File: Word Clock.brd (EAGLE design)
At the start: 32 x 32 mm, 13 parts, among them IC1 DS3231/SO, U1 ATMEGA328P-AU

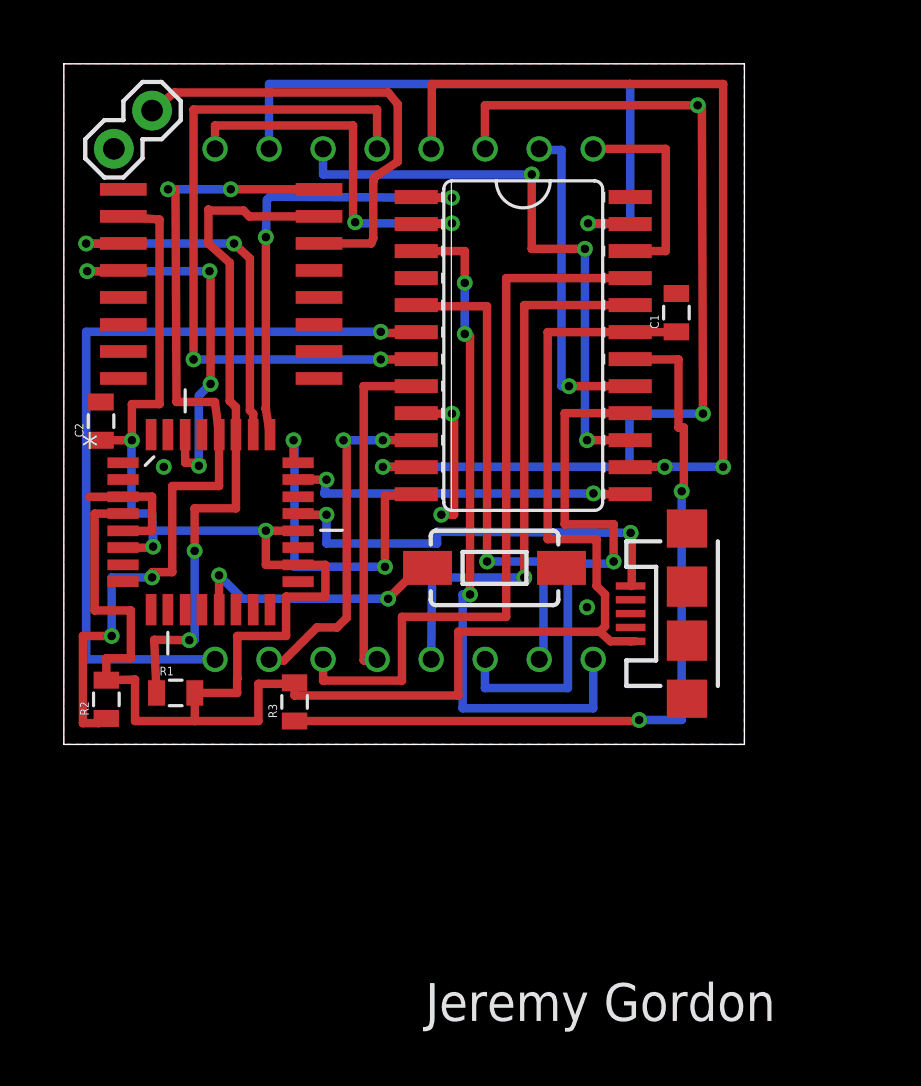
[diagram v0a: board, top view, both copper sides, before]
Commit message: Removed MAX7219, driving with raw atmega.
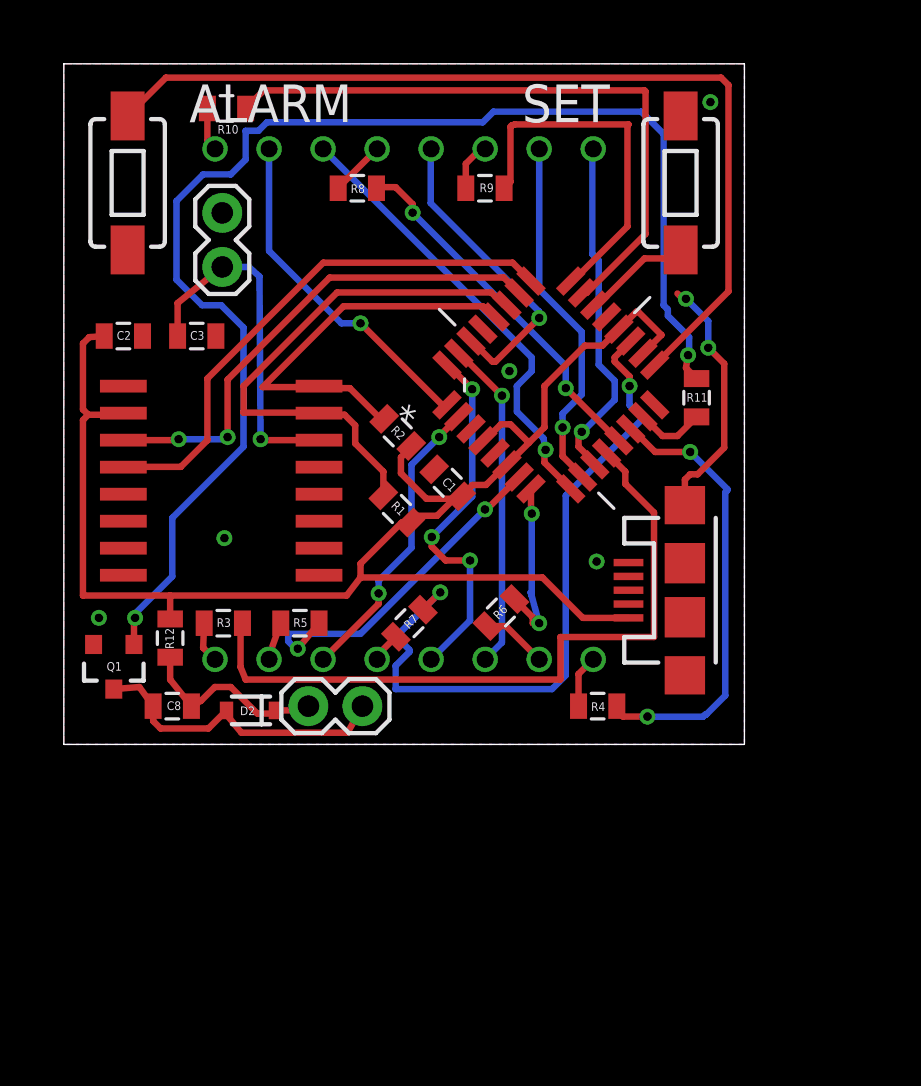
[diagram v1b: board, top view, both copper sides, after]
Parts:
- removed U$1: MAX7219CWG, max7219:SO24L
- added C3, C8: 0.1uF, SparkFun-Capacitors:0805
- added D2: 1N4001, SparkFun-DiscreteSemi:SOD-323
- added JP3: M02PTH, SparkFun-Connectors:1X02
- added Q1: MMBT2222A, SparkFun-DiscreteSemi:SOT23-3
- added R10, R4, R5, R6, R7, R8, R9: 330, SparkFun-Resistors:0805
- added R11: 1k, SparkFun-Resistors:0805
- added R12: 33, SparkFun-Resistors:0805
- added S2: SWITCH-MOMENTARY-2SMD-1101NE, SparkFun-Electromechanical:TACTILE-SWITCH-1101NE
- R3: value 9.53k -> 330
- moved S1 20.1 mm to (29.0, 26.4), turned to 90 degrees
- moved R2 18.6 mm to (15.7, 14.7), turned to 315 degrees
- moved U1 17.3 mm to (22.9, 16.9), turned to 45 degrees
- moved R1 13.5 mm to (15.7, 11.1), turned to 315 degrees
- moved C1 13.4 mm to (18.1, 12.3), turned to 135 degrees
- moved IC1 9.25 mm to (7.40, 12.4)
- moved JP2 8.06 mm to (7.45, 22.4), turned to 90 degrees
- moved R3 4.99 mm to (7.50, 5.70), turned to 0 degrees
- moved C2 4.14 mm to (2.80, 19.2), turned to 0 degrees
- moved JP1 1.10 mm to (29.2, 7.25)
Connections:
- removed net CLK: U$1.13, U1.23
- removed net DIN: U$1.1, U1.25
- removed net LOAD: U$1.12, U1.24
- new net MISO: U1.16
- new net MOSI: R11.2, U1.15
- new net N$20: D1.12, R8.1
- new net N$21: D1.1, R4.1
- new net N$22: D1.7, R5.1
- new net N$23: D1.2, R6.1
- new net N$24: D1.5, R7.1
- new net N$25: D1.9, R10.2
- new net N$26: D1.14, R9.2
- new net N$27: Q1.1, R11.1
- new net N$28: C8.1, D2.C, JP3.1, R12.1
- new net N$29: C8.2, D2.A, JP3.2, Q1.3
- new net RESET: U1.29
- new net SCK: S2.1, U1.17
- net 5V: now also R12.2; no longer R3.2, U$1.19
- net GND: now also C3.2, Q1.2, S2.2; no longer U$1.4, U$1.9
- net N$1: now also D1.13, U1.30; no longer D1.9, U$1.2
- net N$10: now also R10.1, U1.23; no longer D1.3, U$1.16
- net N$11: now also R3.2, U1.12; no longer D1.4, U$1.20
- net N$12: now also R8.2, U1.13; no longer D1.10, U$1.23
- net N$13: now also R4.2, U1.14; no longer D1.6, U$1.21
- net N$14: now also R5.2, U1.7; no longer D1.11, U$1.15
- net N$15: now also R6.2, U1.8; no longer D1.15, U$1.17
- net N$16: now also R7.2, U1.19; no longer D1.16, U$1.22
- net N$17: now also C3.1
- net N$18: now also S1.1, U1.22; no longer R3.1, U$1.18
- net N$19: now also D1.8, R3.1; no longer S1.1, U1.13
- net N$2: now also D1.3, U1.31; no longer D1.14, U$1.11
- net N$3: now also D1.4, U1.32; no longer D1.8, U$1.6
- net N$4: now also D1.10, U1.1; no longer D1.12, U$1.7
- net N$5: now also D1.6, U1.2; no longer D1.1, U$1.3
- net N$6: now also D1.11, U1.9; no longer D1.7, U$1.10
- net N$7: now also D1.15, U1.10; no longer D1.2, U$1.5
- net N$8: now also D1.16, U1.11; no longer D1.5, U$1.8
- net N$9: now also R9.1, U1.24; no longer D1.13, U$1.14
- net RST: now also U1.25; no longer U1.30
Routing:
- net N$27: track 0.00 -> 62.9 mm, vias 0 -> 2
- net SCK: track 0.00 -> 43.7 mm
- net 5V: track 115.7 -> 72.7 mm, vias 3 -> 0
- net N$18: track 37.8 -> 5.87 mm, vias 2 -> 0
- net N$2: track 45.9 -> 15.6 mm, vias 3 -> 1
- net N$16: track 9.89 -> 33.4 mm, vias 0 -> 2
- net SCL: track 41.9 -> 19.4 mm, vias 4 -> 0
- net N$9: track 39.2 -> 17.1 mm, vias 2 -> 0
- net GND: track 33.8 -> 11.9 mm, vias 6 -> 7
- net DIN: track 21.6 -> 0.00 mm, vias 2 -> 0
- net N$3: track 37.0 -> 17.3 mm, vias 1 -> 3
- net N$5: track 32.7 -> 14.1 mm, vias 3 -> 2
- net CLK: track 16.8 -> 0.00 mm, vias 2 -> 0
- net N$4: track 32.8 -> 16.2 mm, vias 2 -> 1
- net LOAD: track 16.4 -> 0.00 mm, vias 2 -> 0
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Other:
- board text added: "ALARM"
- board text added: "SET"
- board text removed: "Jeremy Gordon"

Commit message: Upped isloate and generally tweaked board to be more Cirqoid friendly.
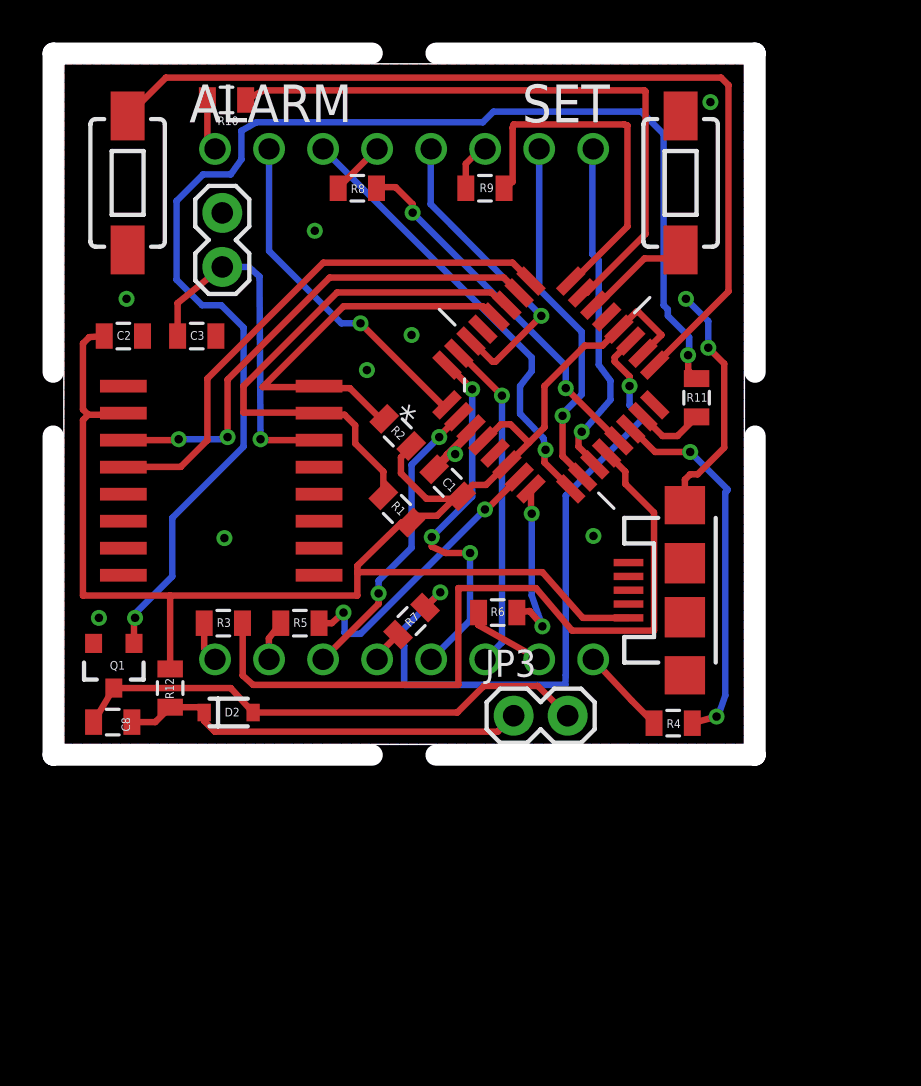
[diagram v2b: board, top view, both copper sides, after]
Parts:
- moved JP3 9.66 mm to (21.1, 1.35)
- moved R4 3.64 mm to (28.6, 1.00)
- moved C8 2.90 mm to (2.30, 1.05)
- moved R12 2.35 mm to (5.00, 2.65)
- moved D2 1.05 mm to (7.75, 1.50), turned to 0 degrees
- moved R10 0.40 mm to (7.65, 30.3)
- moved R6 0.15 mm to (20.4, 6.20), turned to 0 degrees
- moved R7 0.14 mm to (16.4, 5.80)
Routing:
- net N$29: track 14.7 -> 24.8 mm
- net N$28: track 9.55 -> 19.3 mm
- net N$13: track 21.3 -> 17.8 mm
- net N$11: track 33.5 -> 36.7 mm
- net N$14: track 17.0 -> 13.9 mm
- net 5V: track 72.7 -> 75.7 mm
- net GND: track 11.9 -> 14.2 mm, vias 7 -> 11
- net N$21: track 2.49 -> 4.15 mm
- net N$23: track 3.08 -> 3.87 mm
- net N$16: track 33.4 -> 32.7 mm
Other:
- board size 32 x 32 mm -> 33 x 33 mm
